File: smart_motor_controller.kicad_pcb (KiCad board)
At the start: 4 copper layers, 80 x 65 mm, 74 parts, among them J1 I2C_CONN_1, J10 USB_B_Micro, J11 M0_CONN, J12 M1_CONN, J13 M2_CONN, J14 M3_CONN, J2 I2C_CONN_2, J3 Conn_01x02, J4 Conn_02x05_Odd_Even, J5 Conn_01x02, J6 Conn_01x02, J7 Conn_01x02, J8 CAN_CONN, J9 Input 12V, Q1 AO3401A, SW1 SW_SPDT, U1 TPS5430DDA, U2 STM32F405RGT6, U3 USBLC6-2SC6, U4 DRV8871DDA, U5 DRV8871DDA, U6 DRV8871DDA, U7 DRV8871DDA

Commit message: Finish routing
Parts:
- added TP2: 5V, TestPoint:TestPoint_Pad_D2.0mm, F.Cu at (115.2, 56.4)
- added TP3: 3.3V, TestPoint:TestPoint_Pad_D1.5mm, F.Cu at (95.2, 73.8)
- moved R4 25.5 mm to (54.0, 78.5), turned to 90 degrees
- moved C7 3.57 mm to (83.7, 66.0), turned to 180 degrees
- moved C16 3.34 mm to (85.8, 67.6)
- moved C17 3.04 mm to (66.8, 67.2)
- moved C18 3.04 mm to (66.7, 73.0)
- moved C4 3.04 mm to (71.3, 67.0)
- moved C6 3.04 mm to (84.0, 77.5)
- moved HSE1 3.04 mm to (66.7, 70.2)
- moved R6 3.04 mm to (70.0, 71.0)
- moved U2 3.04 mm to (78.0, 72.0)
- moved C15 3.04 mm to (82.6, 79.8)
- moved C3 3.04 mm to (73.5, 63.0)
- moved C5 3.04 mm to (75.1, 79.3)
- moved C8 3.04 mm to (73.7, 64.4)
- moved L2 2.95 mm to (69.6, 76.6)
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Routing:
- net I2C1_SDA: track 2.62 -> 41.8 mm
- net GPIO2: track 0.00 -> 38.8 mm
- net I2C1_SCL: track 2.60 -> 40.2 mm
- net BOOT0: track 0.00 -> 37.5 mm
- net GPIO3: track 0.00 -> 36.3 mm
- net CAN2_RX: track 0.00 -> 35.6 mm, vias 0 -> 1
- net CAN2_TX: track 0.00 -> 33.5 mm, vias 0 -> 1
- net USB_D-: track 0.00 -> 33.1 mm
- net USB_D+: track 0.00 -> 31.5 mm
- net GPIO1: track 0.00 -> 30.9 mm, vias 0 -> 1
- net GPIO0: track 0.00 -> 30.0 mm, vias 0 -> 1
- net I2C3_SCL: track 6.21 -> 35.0 mm, vias 0 -> 2
- net NRST: track 0.00 -> 28.4 mm, vias 0 -> 2
- net M0_OUT2: track 0.00 -> 27.0 mm, vias 0 -> 2
- net M0_OUT1: track 0.00 -> 26.5 mm, vias 0 -> 2
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- added copper zone on B.Cu, net GND
- added copper zone on F.Cu, net GND
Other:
- board text added: "+12V"
- board text added: "0"
- board text added: "12V"
- board text added: "2"
- board text added: "3.3"
- board text added: "3.3V"
- board text added: "5V"
- board text added: "CAN"
- board text added: "GND"
- board text added: "GPIO1"
- board text added: "GPIO3"
- board text added: "M0"
- board text added: "M1"
- board text added: "M2"
- board text added: "M3"
- board text added: "RX"
- board text added: "SCL"
- board text added: "SDA"
- board text added: "TX"
- board text added: "USB"

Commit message: v0.1 Original design
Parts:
- C1: footprint Capacitor_SMD:C_0402_1005Metric -> Capacitor_SMD:C_1206_3216Metric
- C10, C12, C20, C22: value 0.1u -> 100n
- C2: value 0.01u -> 10n
- C9: footprint Capacitor_SMD:C_0402_1005Metric -> Capacitor_SMD:C_0603_1608Metric
- D3: value Red -> BLUE
- R2, R3: footprint Resistor_SMD:R_0402_1005Metric -> Resistor_THT:R_Axial_DIN0204_L3.6mm_D1.6mm_P5.08mm_Horizontal
- R7: value 2k2 -> 100
- R8, R9: footprint Resistor_SMD:R_0402_1005Metric -> Resistor_SMD:R_0603_1608Metric
- moved R3 10.7 mm to (58.8, 75.3), turned to 90 degrees
- moved R2 6.10 mm to (56.4, 75.3), turned to 90 degrees
- moved TP3 3.36 mm to (95.0, 77.1)
- moved C1 2.47 mm to (104.8, 81.3), turned to 0 degrees
- moved J4 1.40 mm to (95.1, 62.8)
- moved R1 1.30 mm to (100.9, 81.9)
- moved R5 1.30 mm to (99.9, 80.8)
- moved R9 1.10 mm to (98.5, 75.0)
- moved C9 0.70 mm to (96.7, 71.8)
- moved R8 0.44 mm to (98.5, 71.8)
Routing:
- net +3V3: track 51.0 -> 58.4 mm, vias 15 -> 16
- net BACK_VSENSE: track 2.70 -> 6.31 mm
- net BOOT0: track 37.5 -> 39.8 mm
- net BACK_EN: track 4.60 -> 3.30 mm
- net I2C1_SDA: track 41.8 -> 42.8 mm
- net I2C1_SCL: track 40.2 -> 39.5 mm
- net SWDIO: track 11.7 -> 11.1 mm
- net NRST: track 28.4 -> 27.8 mm
- net SWCLK: track 13.7 -> 13.1 mm
- net GND: track 83.0 -> 83.2 mm, vias 44 -> 45
- net GPIO0: vias 1 -> 2
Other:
- outline, holes or cut-outs redrawn
- board text added: "+"
- board text added: "1"
- board text added: "3"
- board text added: "4"
- board text added: "5"
- board text added: "BOOT"
- board text added: "I2C"
- board text added: "JLCJLCJLCJLC"
- board text added: "POWER"
- board text added: "RUN"
- board text added: "SWD"
- board text added: "Smart Motor Controller V0.1"
- board text added: "VsReality Robotics"
- board text removed: "GPIO1"
- board text removed: "GPIO3"

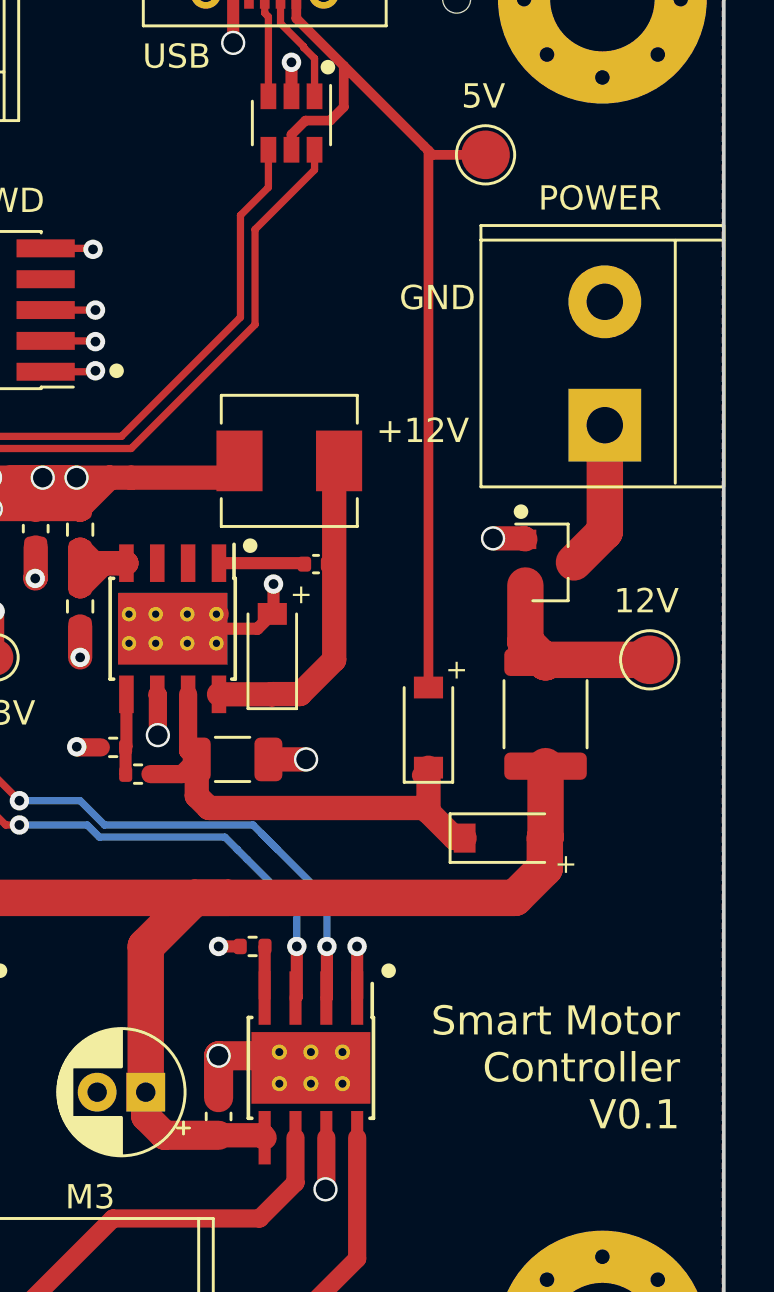
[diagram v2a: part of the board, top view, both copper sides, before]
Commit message: V0.1.1 Removed fuse and AO3401A
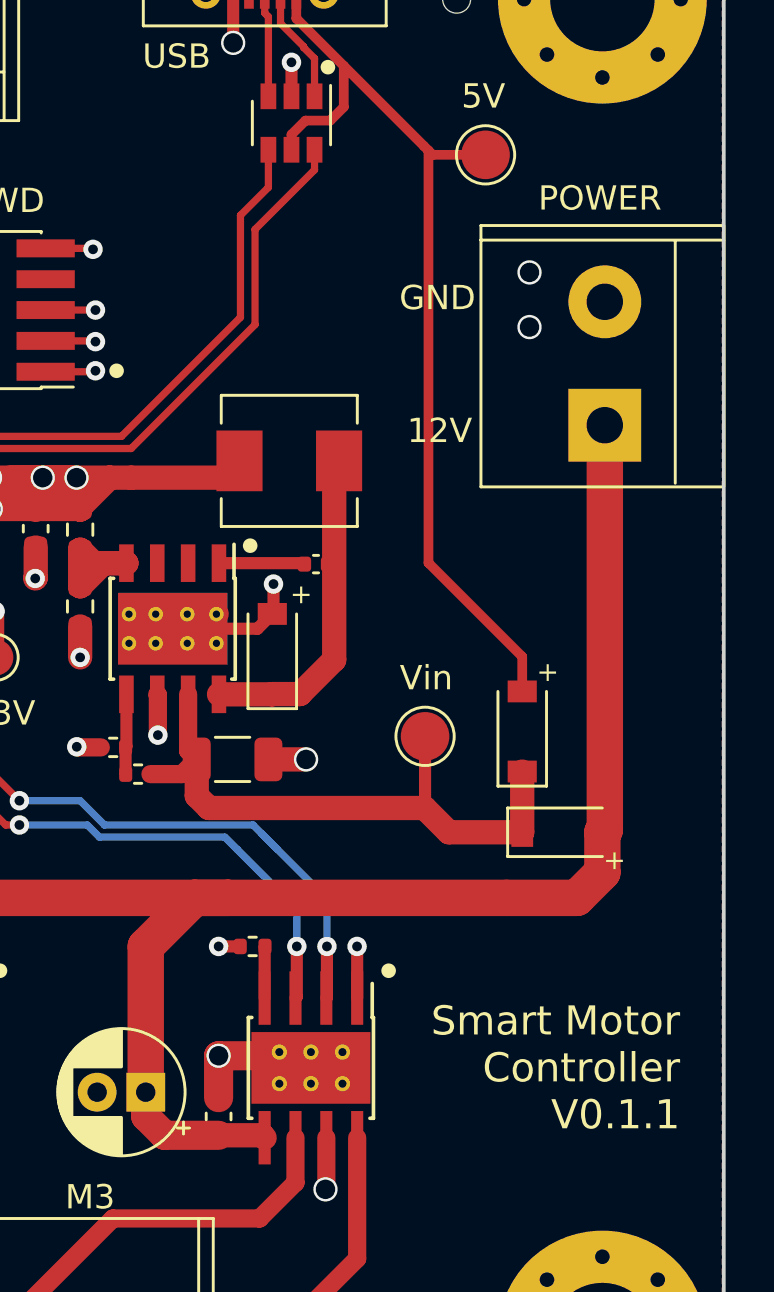
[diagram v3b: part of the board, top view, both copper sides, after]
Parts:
- removed F1: Polyfuse, Fuse:Fuse_1812_4532Metric
- removed Q1: AO3401A, Package_TO_SOT_SMD:SOT-23
- TP1: value 12V -> Vin
- moved TP1 9.77 mm to (112.7, 80.3)
- moved D1 3.86 mm to (116.7, 80.2)
- moved D2 2.38 mm to (118.3, 84.3)
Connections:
- J9 pad 1: +12V -> VM
- TP1 pad 1: Net-(F1-Pad2) -> BACK_IN
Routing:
- net VM: track 129.7 -> 146.9 mm
- net Net-(F1-Pad2): track 7.84 -> 0.00 mm
- net +12V: track 6.18 -> 0.00 mm
- net BACK_IN: track 20.5 -> 26.0 mm
- net +5V: track 38.2 -> 39.9 mm
- net GND: track 83.2 -> 81.9 mm, vias 45 -> 46
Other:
- board text added: "Smart Motor Controller V0.1.1"
- board text added: "Vin"
- board text removed: "+12V"
- board text removed: "Smart Motor Controller V0.1"

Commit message: First draft
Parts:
- removed C1: 10u, Capacitor_SMD:C_1206_3216Metric
- removed C10, C12, C20, C22: 100n, Capacitor_SMD:C_0603_1608Metric
- removed C11, C19, C21, C23: 47u, Capacitor_THT:CP_Radial_D5.0mm_P2.00mm
- removed C2: 10n, Capacitor_SMD:C_0402_1005Metric
- removed C9: 22u, Capacitor_SMD:C_0603_1608Metric
- removed D4: B5819W, Diode_SMD:D_SOD-123
- removed J1: I2C_CONN_1, VsReality_Footprints:DB128L_5.08_2P_GN_S
- removed J11: M0_CONN, VsReality_Footprints:DB128L_5.08_2P_GN_S
- removed J12: M1_CONN, VsReality_Footprints:DB128L_5.08_2P_GN_S
- removed J13: M2_CONN, VsReality_Footprints:DB128L_5.08_2P_GN_S
- removed J14: M3_CONN, VsReality_Footprints:DB128L_5.08_2P_GN_S
- removed J2: I2C_CONN_2, VsReality_Footprints:DB128L_5.08_2P_GN_S
- removed J3, J5, J6, J7: Conn_01x02, Connector_PinHeader_2.54mm:PinHeader_1x02_P2.54mm_Vertical
- removed J8: CAN_CONN, VsReality_Footprints:DB128L_5.08_2P_GN_S
- removed L1: 10u, Inductor_SMD:L_Sunlord_MWSA0518_5.4x5.2mm
- removed R1, R5: 100K, Resistor_SMD:R_0402_1005Metric
- removed R10, R11, R12, R13: 68K, Resistor_SMD:R_0402_1005Metric
- removed R4: 10k, Resistor_SMD:R_0402_1005Metric
- removed R8: 51K, Resistor_SMD:R_0603_1608Metric
- removed R9: 30K, Resistor_SMD:R_0603_1608Metric
- removed SW1: SW_SPDT, VsReality_Footprints:SW_SPDT
- removed TP3: 3.3V, TestPoint:TestPoint_Pad_D1.5mm
- removed U1: TPS5430DDA, Package_SO:TI_SO-PowerPAD-8_ThermalVias
- removed U4, U5, U6, U7: DRV8871DDA, Package_SO:Texas_HTSOP-8-1EP_3.9x4.9mm_P1.27mm_EP2.95x4.9mm_Mask2.4x3.1mm_ThermalVias
- added C101: 1u, Capacitor_SMD:C_0402_1005Metric, F.Cu at (202.8, 35.5)
- added C201: 100nf, Capacitor_SMD:C_0402_1005Metric, F.Cu at (193.4, 112.5)
- added C202: 10uf, Capacitor_SMD:C_1206_3216Metric, F.Cu at (180.5, 66.4)
- added C203: 10nf, Capacitor_SMD:C_0603_1608Metric, F.Cu at (161.3, 123.5)
- added C204: 1nF, Capacitor_SMD:C_0402_1005Metric, F.Cu at (193.4, 114.5)
- added C205: 8.2nF, Capacitor_SMD:C_0603_1608Metric, F.Cu at (161.3, 127.4)
- added C206: 47uF, Capacitor_SMD:C_1206_3216Metric, F.Cu at (152.0, 130.5)
- added C207: 47uF, Capacitor_SMD:C_1206_3216Metric, F.Cu at (180.3, 74.0)
- added C301: 100n, Capacitor_SMD:C_0603_1608Metric, F.Cu at (116.5, 102.5)
- added C302: 47u, Capacitor_THT:CP_Radial_D5.0mm_P2.00mm, F.Cu at (117.0, 98.5)
- added C303: 100n, Capacitor_SMD:C_0603_1608Metric, F.Cu at (130.0, 102.5)
- added C304: 47u, Capacitor_THT:CP_Radial_D5.0mm_P2.00mm, F.Cu at (130.5, 98.5)
- added C305: 100n, Capacitor_SMD:C_0603_1608Metric, F.Cu at (144.0, 102.5)
- added C306: 47u, Capacitor_THT:CP_Radial_D5.0mm_P2.00mm, F.Cu at (144.5, 98.5)
- added C307: 100n, Capacitor_SMD:C_0603_1608Metric, F.Cu at (158.0, 102.0)
- added C308: 47u, Capacitor_THT:CP_Radial_D5.0mm_P2.00mm, F.Cu at (158.0, 98.0)
- added D201: B5819W, Diode_SMD:D_SOD-123, F.Cu at (180.0, 127.0)
- added H5: MountingHole_Pad, MountingHole:MountingHole_2.7mm_M2.5_Pad, F.Cu at (164.5, 54.5)
- added H6: MountingHole_Pad, MountingHole:MountingHole_2.7mm_M2.5_Pad, F.Cu at (164.5, 112.5)
- added J101: Conn_02x04_Odd_Even, Connector_PinHeader_2.54mm:PinHeader_2x04_P2.54mm_Vertical, F.Cu at (165.0, 68.0)
- added J102: I2C_CONN, Connector_JST:JST_PH_S4B-PH-SM4-TB_1x04-1MP_P2.00mm_Horizontal, F.Cu at (140.0, 36.0)
- added J103: CAN_CONN, Connector_JST:JST_PH_S2B-PH-SM4-TB_1x02-1MP_P2.00mm_Horizontal, F.Cu at (154.0, 36.0)
- added J301: M0_CONN, VsReality_Footprints:DB128L_5.08_2P_GN_S, F.Cu at (125.5, 111.0)
- added J302: M1_CONN, VsReality_Footprints:DB128L_5.08_2P_GN_S, F.Cu at (145.5, 111.0)
- added J303: M2_CONN, VsReality_Footprints:DB128L_5.08_2P_GN_S, F.Cu at (135.5, 111.0)
- added J304: M3_CONN, VsReality_Footprints:DB128L_5.08_2P_GN_S, F.Cu at (155.5, 111.0)
- added J305: E0_CONN, Connector_PinHeader_2.54mm:PinHeader_1x04_P2.54mm_Vertical, F.Cu at (165.0, 75.0)
- added J306: E1_CONN, Connector_PinHeader_2.54mm:PinHeader_1x04_P2.54mm_Vertical, F.Cu at (165.0, 78.5)
- added J307: E2_CONN, Connector_PinHeader_2.54mm:PinHeader_1x04_P2.54mm_Vertical, F.Cu at (165.0, 82.0)
- added J308: E3_CONN, Connector_PinHeader_2.54mm:PinHeader_1x04_P2.54mm_Vertical, F.Cu at (165.0, 85.5)
- added J309: V Encoders jamper, Connector_PinHeader_2.54mm:PinHeader_1x03_P2.54mm_Vertical, F.Cu at (141.5, 84.0)
- added J310: V Encoders external, VsReality_Footprints:DB128L_5.08_2P_GN_S, F.Cu at (117.0, 70.0)
- added L201: 10uH, Inductor_SMD:L_Sunlord_MWSA0518_5.4x5.2mm, F.Cu at (137.5, 77.0)
- added Q101: FDD6685, Package_TO_SOT_SMD:TO-252-2, F.Cu at (127.5, 80.4)
- added R101: 10k, Resistor_SMD:R_0402_1005Metric, F.Cu at (200.0, 35.5)
- added R201: 10K, Resistor_SMD:R_0402_1005Metric, F.Cu at (191.5, 109.4)
- added R202: 30K, Resistor_SMD:R_0603_1608Metric, F.Cu at (188.3, 107.1)
- added R203: 3.3K, Resistor_SMD:R_0402_1005Metric, F.Cu at (191.5, 111.3)
- added R301: 30K, Resistor_SMD:R_0603_1608Metric, F.Cu at (196.2, 95.3)
- added R302: 30K, Resistor_SMD:R_0603_1608Metric, F.Cu at (180.0, 103.0)
- added R303: 30K, Resistor_SMD:R_0603_1608Metric, F.Cu at (189.1, 95.7)
- added R304: 30K, Resistor_SMD:R_0603_1608Metric, F.Cu at (198.7, 95.4)
- added U301: DRV8871DDA, Package_SO:Texas_HTSOP-8-1EP_3.9x4.9mm_P1.27mm_EP2.95x4.9mm_Mask2.4x3.1mm_ThermalVias, F.Cu at (122.6, 98.9)
- added U302: DRV8871DDA, Package_SO:Texas_HTSOP-8-1EP_3.9x4.9mm_P1.27mm_EP2.95x4.9mm_Mask2.4x3.1mm_ThermalVias, F.Cu at (150.1, 99.0)
- added U303: DRV8871DDA, Package_SO:Texas_HTSOP-8-1EP_3.9x4.9mm_P1.27mm_EP2.95x4.9mm_Mask2.4x3.1mm_ThermalVias, F.Cu at (136.0, 98.9)
- added U304: DRV8871DDA, Package_SO:Texas_HTSOP-8-1EP_3.9x4.9mm_P1.27mm_EP2.95x4.9mm_Mask2.4x3.1mm_ThermalVias, F.Cu at (163.5, 98.9)
- H1, H2, H3, H4: footprint MountingHole:MountingHole_4.3mm_M4_Pad_Via -> MountingHole:MountingHole_2.7mm_M2.5_Pad
- moved R3 162.3 mm to (220.9, 84.0)
- moved R2 162.3 mm to (218.4, 84.0)
- moved H1 134.5 mm to (164.5, 34.5), turned to 90 degrees
- moved TP1 113.9 mm to (224.3, 103.0)
- moved D2 110.8 mm to (227.0, 62.5)
- moved R14 109.0 mm to (178.5, 33.1), turned to 270 degrees
- moved D1 108.4 mm to (222.5, 56.5)
- moved R15 101.9 mm to (178.5, 39.1), turned to 90 degrees
- moved H3 90.5 mm to (115.5, 112.5), turned to 90 degrees
- moved TP2 86.9 mm to (195.0, 22.0)
- moved H4 70.6 mm to (115.5, 34.5), turned to 90 degrees
- moved C17 66.9 mm to (132.4, 53.9)
- moved C18 66.9 mm to (132.3, 59.7)
- moved C3 66.9 mm to (139.1, 49.6)
- moved C6 66.9 mm to (149.6, 64.2)
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- renumbered J4 to J104
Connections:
- net Net-(U2-Pad51) renamed USART3_TX
- net Net-(U2-Pad52) renamed USART3_RX
- D2 pad 2: VM -> VMOTORS
- J9 pad 1: VM -> +12V
- R14 pad 2: I2C3_SCL -> I2C2_SCL
- R15 pad 2: I2C3_SDA -> I2C2_SDA
- U2 pad 14: M0_OUT1 -> ENCODER_3_A
- U2 pad 15: M0_OUT2 -> ENCODER_3_B
- U2 pad 16: M1_OUT1 -> GPIO0
- U2 pad 17: M1_OUT2 -> GPIO1
- U2 pad 20: Net-(U2-Pad20) -> GPIO2
- U2 pad 21: M2_OUT1 -> GPIO3
- U2 pad 22: Net-(U2-Pad22) -> ENCODER_1_A
- U2 pad 23: Net-(U2-Pad23) -> ENCODER_1_B
- U2 pad 29: M3_OUT1 -> I2C2_SCL
- U2 pad 30: M3_OUT2 -> I2C2_SDA
- U2 pad 35: Net-(U2-Pad35) -> M3_OUT1
- U2 pad 36: Net-(U2-Pad36) -> M3_OUT2
- U2 pad 37: Net-(U2-Pad37) -> M1_OUT1
- U2 pad 38: Net-(U2-Pad38) -> M1_OUT2
- U2 pad 39: Net-(U2-Pad39) -> M2_OUT1
- U2 pad 40: Net-(U2-Pad40) -> M2_OUT2
- U2 pad 41: I2C3_SCL -> M0_OUT1
- U2 pad 42: I2C3_SDA -> M0_OUT2
- U2 pad 50: Net-(U2-Pad50) -> ENCODER_0_A
- U2 pad 55: M2_OUT2 -> ENCODER_0_B
- U2 pad 56: GPIO3 -> Net-(U2-Pad56)
- U2 pad 57: GPIO2 -> Net-(U2-Pad57)
- U2 pad 58: I2C1_SCL -> ENCODER_2_A
- U2 pad 59: I2C1_SDA -> ENCODER_2_B
- U2 pad 61: GPIO1 -> I2C1_SCL
- U2 pad 62: GPIO0 -> I2C1_SDA
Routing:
- net VM: track 146.9 -> 0.00 mm
- net GPIO2: track 38.8 -> 0.00 mm
- net M3_OUT2: track 38.7 -> 0.00 mm, vias 2 -> 0
- net GND: track 81.9 -> 44.2 mm, vias 46 -> 31
- net M3_OUT1: track 37.7 -> 2.15 mm
- net I2C3_SCL: track 35.0 -> 0.00 mm, vias 2 -> 0
- net CAN2_TX: track 34.0 -> 0.81 mm, vias 1 -> 0
- net USB_D-: track 33.1 -> 0.00 mm
- net +3V3: track 58.4 -> 25.7 mm, vias 16 -> 11
- net I2C3_SDA: track 32.6 -> 0.00 mm, vias 2 -> 0
- net GPIO3: track 36.3 -> 4.79 mm, vias 0 -> 1
- net USB_D+: track 31.5 -> 0.00 mm
- net +5V: track 39.9 -> 8.73 mm
- net M2_OUT2: track 30.6 -> 0.00 mm, vias 2 -> 0
- net CAN2_RX: track 35.6 -> 6.14 mm, vias 1 -> 0
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- removed copper zone on In2.Cu, net +3V3
- removed copper zone on B.Cu, net GND
- removed copper zone on F.Cu, net GND
- removed copper zone on In1.Cu, net GND
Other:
- board size 80 x 65 mm -> 56 x 85 mm

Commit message: Layout
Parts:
- removed J305: E0_CONN, Connector_PinHeader_2.54mm:PinHeader_1x04_P2.54mm_Vertical
- removed J306: E1_CONN, Connector_PinHeader_2.54mm:PinHeader_1x04_P2.54mm_Vertical
- removed J307: E2_CONN, Connector_PinHeader_2.54mm:PinHeader_1x04_P2.54mm_Vertical
- removed J308: E3_CONN, Connector_PinHeader_2.54mm:PinHeader_1x04_P2.54mm_Vertical
- removed R2, R3: 2k2, Resistor_THT:R_Axial_DIN0204_L3.6mm_D1.6mm_P5.08mm_Horizontal
- added 3.3V201: TestPoint_Small, TestPoint:TestPoint_Pad_D1.5mm, F.Cu at (165.0, 41.0)
- added D301: B5819W, Diode_SMD:D_SOD-123, F.Cu at (161.0, 60.9)
- added SW102: SW_NRST, VsReality_Footprints:Diptronics MPTFP2-V-TR SMD 2.9x3.9x2mm, F.Cu at (157.9, 47.8)
- added SW103: SW_NRST, VsReality_Footprints:Diptronics MPTFP2-V-TR SMD 2.9x3.9x2mm, F.Cu at (127.9, 47.6)
- added U201: TPS54331DDAR, VsReality_Footprints:Texas_Instruments-DDAR-PDSO-G8-12_2011-F-0, F.Cu at (141.6, 82.6)
- J101: value Conn_02x04_Odd_Even -> Breakout; footprint Connector_PinHeader_2.54mm:PinHeader_2x04_P2.54mm_Vertical -> Connector_PinHeader_2.54mm:PinHeader_2x06_P2.54mm_Vertical
- J104: value Conn_02x05_Odd_Even -> Debug; footprint Connector_PinHeader_1.27mm:PinHeader_2x05_P1.27mm_Vertical_SMD -> Connector_PinHeader_2.54mm:PinHeader_1x04_P2.54mm_Vertical
- J301, J302, J303, J304, J9: footprint VsReality_Footprints:DB128L_5.08_2P_GN_S -> VsReality_Footprints:Ningbo_Kangnex_Elec_WJ128V_5_0_2P
- J309: value V Encoders jamper -> External encoders power; footprint Connector_PinHeader_2.54mm:PinHeader_1x03_P2.54mm_Vertical -> Connector_PinHeader_2.54mm:PinHeader_1x02_P2.54mm_Vertical
- J310: value V Encoders external -> Encoder Commector; footprint VsReality_Footprints:DB128L_5.08_2P_GN_S -> VsReality_Footprints:Encoder_PinHeader_4x04_P2.54mm_Vertical
- TP1: footprint TestPoint:TestPoint_Pad_D2.0mm -> TestPoint:TestPoint_Pad_D1.5mm
- moved TP1 98.2 mm to (127.5, 86.5)
- moved D2 96.5 mm to (132.8, 83.6), turned to 270 degrees
- moved D1 92.4 mm to (132.8, 78.8)
- moved C101 77.8 mm to (126.4, 49.8)
- moved R301 77.5 mm to (118.8, 91.7), turned to 270 degrees
- moved TP2 67.1 mm to (131.0, 42.0)
- moved C201 64.2 mm to (138.5, 79.2)
- moved D201 61.0 mm to (143.0, 78.5), turned to 180 degrees
- moved R303 58.0 mm to (131.2, 91.7), turned to 270 degrees
- moved C206 55.3 mm to (143.8, 75.8), turned to 180 degrees
- moved C204 53.8 mm to (149.6, 83.2)
- moved R203 52.0 mm to (146.6, 85.0), turned to 270 degrees
- moved J101 51.1 mm to (114.5, 60.0), turned to 0 degrees
- moved J310 50.1 mm to (165.5, 82.5), turned to 180 degrees
- moved R201 49.7 mm to (148.4, 84.6), turned to 180 degrees
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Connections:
- C204 pad 1: Net-(C204-Pad1) -> Net-(C203-Pad1)
- C204 pad 2: GND -> Net-(C204-Pad2)
- J101 pad 1: +3V3 -> GND
- J101 pad 2: GND -> +3V3
- J104 pad 1: +3V3 -> GND
- J104 pad 2: SWDIO -> SWCLK
- J104 pad 3: GND -> SWDIO
- J104 pad 4: SWCLK -> NRST
- J309 pad 1: +3V3 -> GND
- J310 pad 1: Net-(J309-Pad3) -> GND
- J310 pad 2: GND -> V_ENCODER
- J9 pad 1: +12V -> GND
- J9 pad 2: GND -> +12V
- R202 pad 1: Net-(C203-Pad1) -> Net-(C204-Pad2)
- R202 pad 2: Net-(C204-Pad1) -> GND
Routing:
- net VMOTORS: track 2.14 -> 135.0 mm, vias 2 -> 0
- net GND: track 44.2 -> 99.0 mm, vias 31 -> 51
- net M3_OUT2: track 0.00 -> 38.1 mm
- net +3V3: track 25.7 -> 62.2 mm, vias 11 -> 12
- net M3_OUT1: track 2.15 -> 36.9 mm, vias 2 -> 0
- net GPIO2: track 0.00 -> 29.8 mm
- net CAN2_TX: track 0.81 -> 29.6 mm, vias 0 -> 2
- net V_ENCODER: track 0.00 -> 24.8 mm
- net CAN2_RX: track 6.14 -> 29.5 mm, vias 0 -> 2
- net Net-(C201-Pad2): track 0.00 -> 22.9 mm, vias 0 -> 2
- net GPIO3: track 4.79 -> 27.3 mm, vias 1 -> 0
- net I2C1_SDA: track 24.8 -> 2.32 mm, vias 2 -> 1
- net ENCODER_1_A: track 0.00 -> 21.7 mm
- net ENCODER_1_B: track 0.00 -> 20.1 mm
- net GPIO0: track 5.33 -> 24.1 mm, vias 1 -> 0
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- added copper zone on In1.Cu, net +3V3
- added copper zone on B.Cu, net GND
- added copper zone on F.Cu, net GND
- added copper zone on In2.Cu, net GND
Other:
- board text added: "0|1"
- board text added: "A"
- board text added: "B"
- board text added: "CLK"
- board text added: "IO"
- board text added: "NRST"
- board text added: "Smart Motor Controller V0.2"
- board text added: "USART"
- board text added: "VE"
- board text removed: "Smart Motor Controller V0.1.1"

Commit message: Additional changes
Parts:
- moved H4 83.6 mm to (193.9, 63.6), turned to 0 degrees
- moved H1 83.5 mm to (193.9, 112.6), turned to 0 degrees
- moved J10 80.4 mm to (195.1, 73.8), turned to 90 degrees
- moved J103 76.8 mm to (192.4, 103.1), turned to 90 degrees
- moved J104 76.7 mm to (187.9, 62.6), turned to 270 degrees
- moved 3.3V201 75.5 mm to (187.4, 113.1), turned to 270 degrees
- moved J102 73.9 mm to (192.4, 88.6), turned to 90 degrees
- moved R14 70.3 mm to (177.4, 100.9), turned to 90 degrees
- moved U3 69.0 mm to (187.1, 74.9), turned to 180 degrees
- moved R15 65.7 mm to (177.4, 98.7), turned to 270 degrees
- moved TP2 65.5 mm to (185.0, 79.1), turned to 270 degrees
- moved C17 63.9 mm to (180.6, 92.9), turned to 180 degrees
- moved SW102 62.5 mm to (180.6, 106.0), turned to 270 degrees
- moved HSE1 60.6 mm to (180.7, 89.9), turned to 90 degrees
- moved C3 60.3 mm to (173.9, 97.2), turned to 0 degrees
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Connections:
- J101 pad 7: I2C1_SDA -> I2C2_SDA
- J101 pad 8: I2C1_SCL -> I2C2_SCL
- J102 pad 2: I2C3_SDA -> I2C1_SCL
- J102 pad 3: I2C3_SCL -> I2C1_SDA
- R14 pad 2: I2C2_SCL -> I2C1_SCL
- R15 pad 2: I2C2_SDA -> I2C1_SDA
- TP1 pad 1: BACK_IN -> VMOTORS
- U2 pad 35: M3_OUT1 -> M0_OUT1
- U2 pad 36: M3_OUT2 -> M0_OUT2
- U2 pad 37: M1_OUT1 -> M2_OUT1
- U2 pad 38: M1_OUT2 -> M2_OUT2
- U2 pad 39: M2_OUT1 -> M1_OUT1
- U2 pad 40: M2_OUT2 -> M1_OUT2
- U2 pad 41: M0_OUT1 -> M3_OUT1
- U2 pad 42: M0_OUT2 -> M3_OUT2
- U201 pad ~: (no net) -> GND
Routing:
- net +5V: track 8.73 -> 50.4 mm, vias 0 -> 2
- net SWCLK: track 2.58 -> 41.4 mm, vias 0 -> 2
- net USART3_TX: track 0.00 -> 36.5 mm, vias 0 -> 2
- net M1_OUT1: track 0.02 -> 35.8 mm, vias 0 -> 2
- net M1_OUT2: track 0.01 -> 35.3 mm, vias 0 -> 2
- net SWDIO: track 3.61 -> 38.3 mm, vias 0 -> 2
- net USB_D-: track 0.00 -> 33.5 mm, vias 0 -> 2
- net USB_D+: track 0.00 -> 33.4 mm, vias 0 -> 2
- net I2C1_SCL: track 0.00 -> 33.4 mm
- net ENCODER_3_B: track 7.84 -> 40.7 mm, vias 1 -> 2
- net USART3_RX: track 0.00 -> 32.5 mm, vias 0 -> 2
- net ENCODER_3_A: track 7.14 -> 36.6 mm, vias 1 -> 2
- net I2C1_SDA: track 2.32 -> 31.7 mm, vias 1 -> 0
- net M2_OUT2: track 0.00 -> 28.7 mm, vias 0 -> 2
- net M2_OUT1: track 0.00 -> 28.5 mm, vias 0 -> 2
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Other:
- board size 56 x 85 mm -> 85 x 56 mm
- board text removed: "0|1"
- board text removed: "12V"
- board text removed: "4"
- board text removed: "5"
- board text removed: "RUN"
- board text removed: "RX"
- board text removed: "SWD"
- board text removed: "TX"

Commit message: Change footprint for a comonent
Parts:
- R301, R302, R303, R304: value 30K -> 0.15
- U201: footprint VsReality_Footprints:Texas_Instruments-DDAR-PDSO-G8-12_2011-F-0 -> Package_SO:HSOP-8-1EP_3.9x4.9mm_P1.27mm_EP2.41x3.1mm_ThermalVias
- U301, U302, U303, U304: value DRV8871DDA -> DRV8870DDA
- moved R301 9.77 mm to (128.0, 71.3)
- moved R303 9.73 mm to (128.0, 83.7)
- moved R302 9.73 mm to (128.0, 96.1)
- moved R304 9.73 mm to (128.0, 108.5)
- moved U301 0.10 mm to (133.9, 70.7)
- moved U302 0.10 mm to (133.9, 95.5)
- moved U303 0.10 mm to (133.9, 83.1)
- moved U304 0.10 mm to (133.9, 107.9)
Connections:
- U301 pad 4: Net-(R301-Pad1) -> +3V3
- U301 pad 7: GND -> Net-(R301-Pad1)
- U302 pad 4: Net-(R302-Pad1) -> +3V3
- U302 pad 7: GND -> Net-(R302-Pad1)
- U303 pad 4: Net-(R303-Pad1) -> +3V3
- U303 pad 7: GND -> Net-(R303-Pad1)
- U304 pad 4: Net-(R304-Pad1) -> +3V3
- U304 pad 7: GND -> Net-(R304-Pad1)
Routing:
- net GND: track 114.1 -> 106.8 mm, vias 64 -> 62
- net +3V3: track 67.3 -> 73.5 mm, vias 15 -> 19
